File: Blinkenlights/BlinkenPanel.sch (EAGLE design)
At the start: 33 parts, among them IC3 MCP23017SS

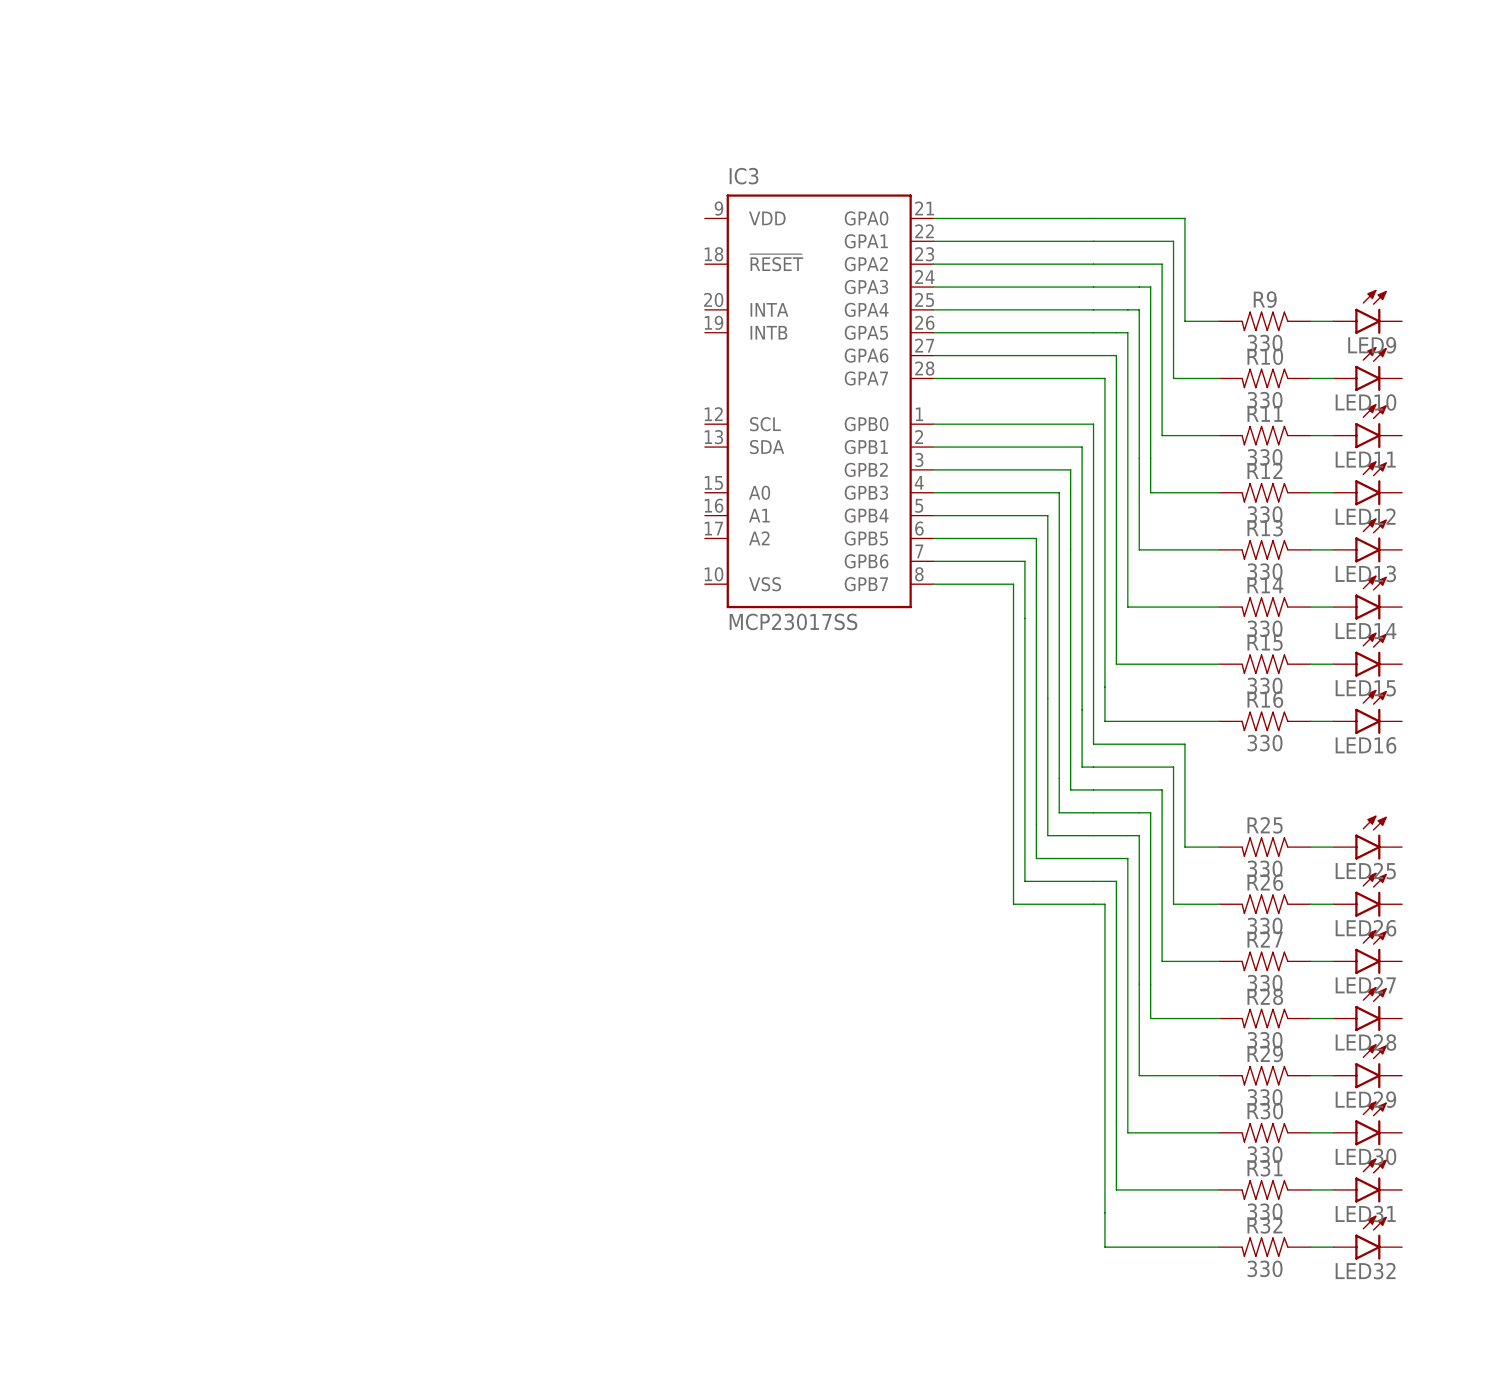
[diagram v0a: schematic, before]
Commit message: added prints, fixed blinkenpanel
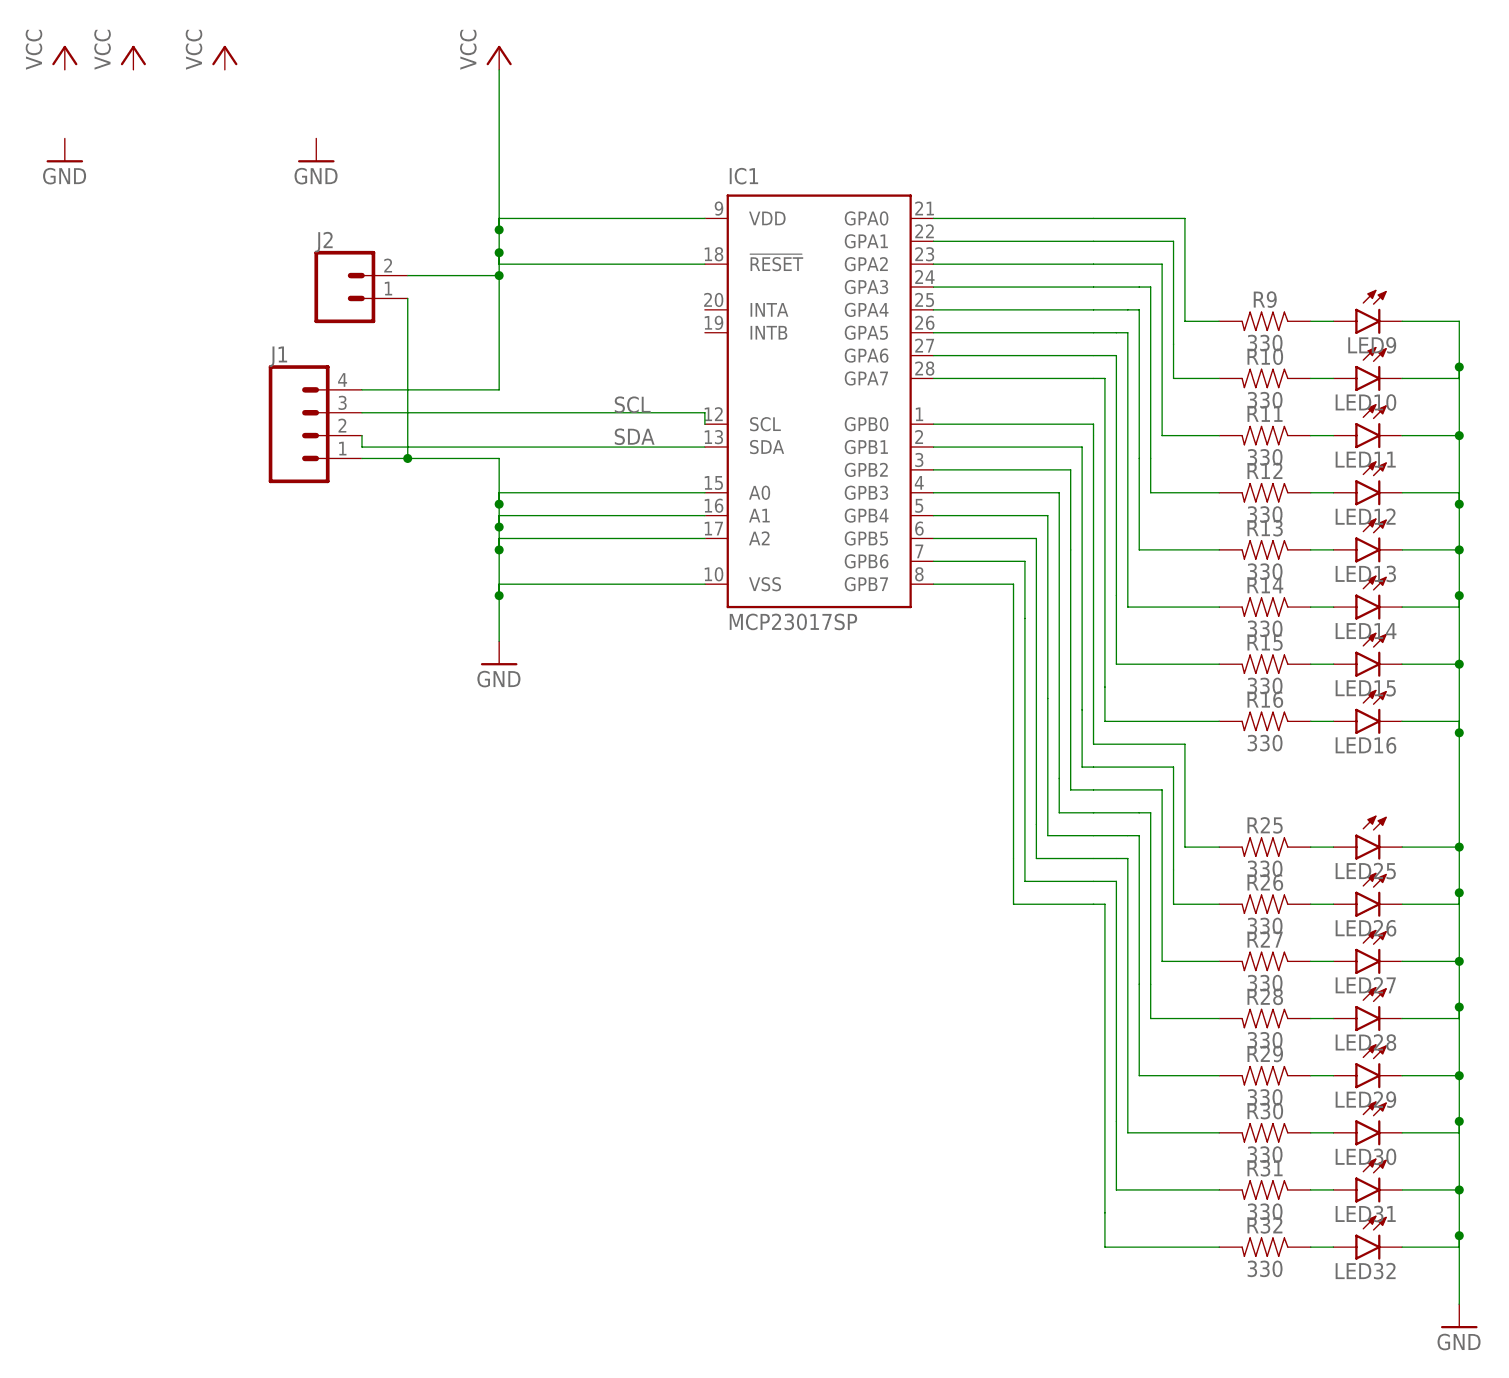
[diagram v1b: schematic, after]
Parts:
- removed IC3: MCP23017SS, microchip:MCP23017SS
- added IC1: MCP23017SP, microchip:MCP23017SP
- added J1: (no value), SparkFun-Connectors:CONN_04LOCK
- added J2: (no value), SparkFun-Connectors:CONN_02
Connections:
- new net GND: IC1.A0, IC1.A1, IC1.A2, IC1.VSS, J1.1, J2.1, LED10.C, LED11.C, LED12.C, LED13.C, LED14.C, LED15.C, LED16.C, LED25.C, LED26.C, LED27.C, LED28.C, LED29.C, LED30.C, LED31.C, LED32.C, LED9.C
- new net SCL: IC1.SCL, J1.3
- new net SDA: IC1.SDA, J1.2
- new net VCC: IC1.!RESET, IC1.VDD, J1.4, J2.2
- net N$25: now also IC1.GPA0; no longer IC3.GPA0
- net N$26: now also IC1.GPA1; no longer IC3.GPA1
- net N$27: now also IC1.GPA2; no longer IC3.GPA2
- net N$28: now also IC1.GPA3; no longer IC3.GPA3
- net N$29: now also IC1.GPA4; no longer IC3.GPA4
- net N$30: now also IC1.GPA5; no longer IC3.GPA5
- net N$31: now also IC1.GPA6; no longer IC3.GPA6
- net N$32: now also IC1.GPA7; no longer IC3.GPA7
- net N$57: now also IC1.GPB0; no longer IC3.GPB0
- net N$58: now also IC1.GPB1; no longer IC3.GPB1
- net N$59: now also IC1.GPB2; no longer IC3.GPB2
- net N$60: now also IC1.GPB3; no longer IC3.GPB3
- net N$61: now also IC1.GPB4; no longer IC3.GPB4
- net N$62: now also IC1.GPB5; no longer IC3.GPB5
- net N$63: now also IC1.GPB6; no longer IC3.GPB6
- net N$64: now also IC1.GPB7; no longer IC3.GPB7
